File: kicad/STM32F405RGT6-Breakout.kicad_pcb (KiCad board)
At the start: 4 copper layers, 58 parts, among them J1 USB_C_Receptacle_USB2.0, J2 PWR OUT, J3 SWD/JTAG, J4 USART6, J5 SPI1, J6 I2C1, J7 I2C2, Q1 Si2301CDS, SW1 TS-1187A-B-A-B, SW2 TS-1187A-B-A-B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

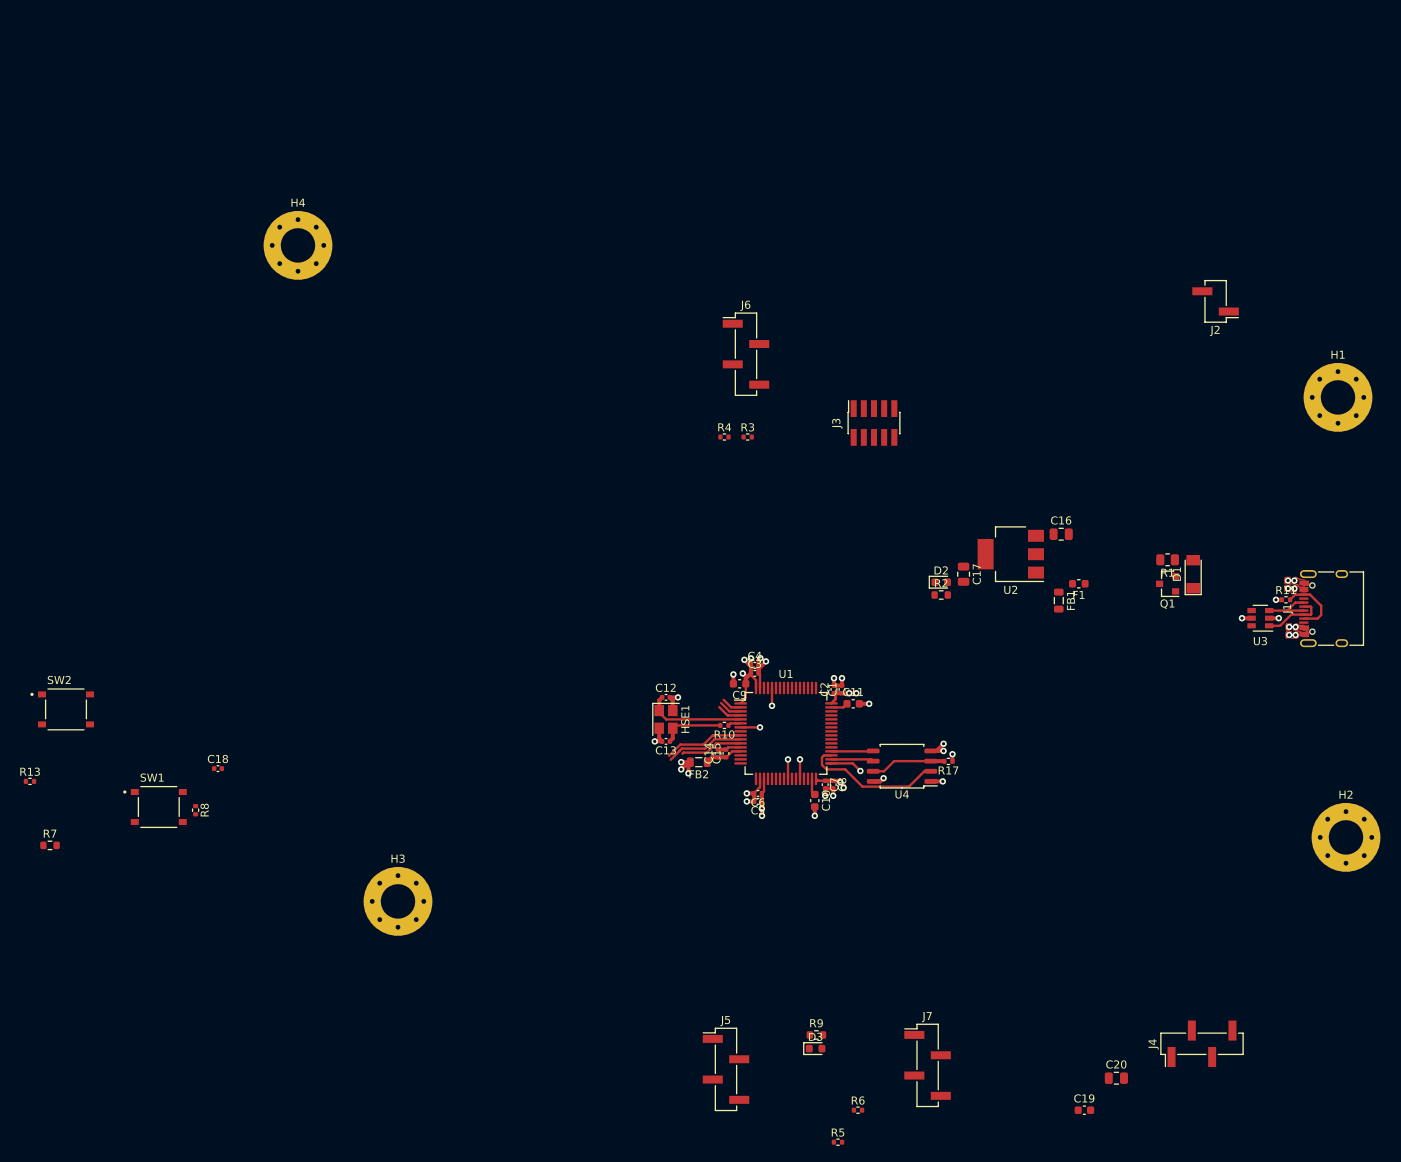
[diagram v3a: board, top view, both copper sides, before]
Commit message: - Lots of GPIO breakouts wired up - Lots of signal isolation vias that I'm completely guessing about
Still to lay out and route: power, USB, UART, SWD
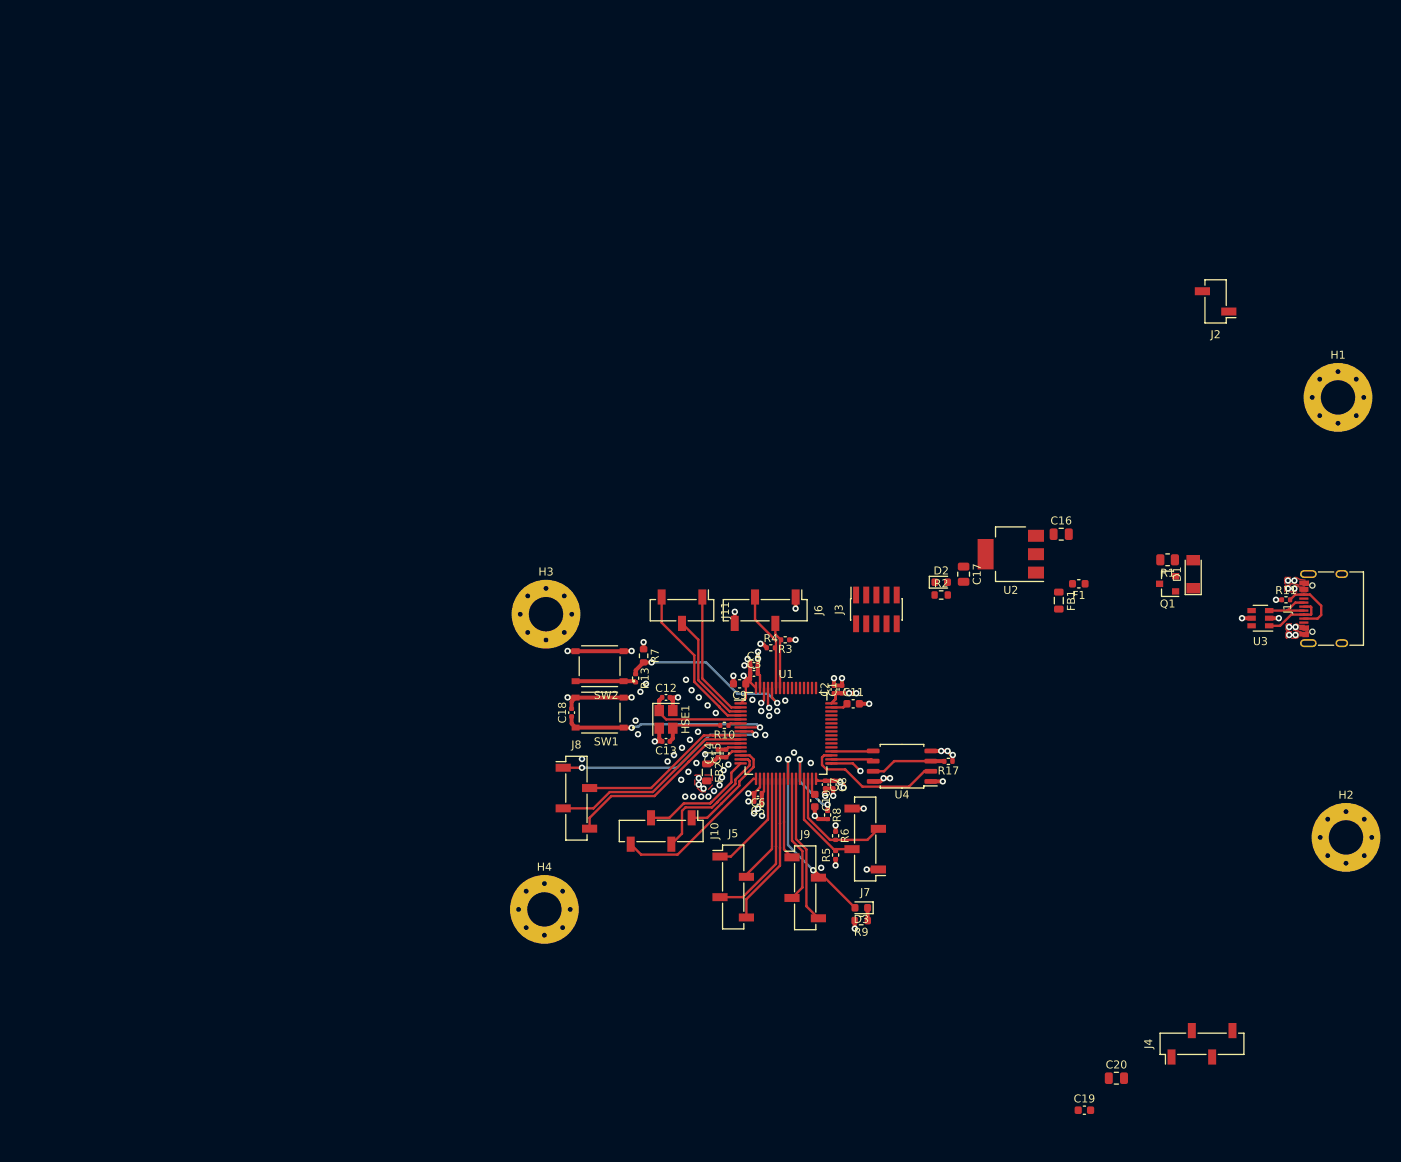
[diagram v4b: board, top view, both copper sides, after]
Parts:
- added J10: Conn_01x04, Connector_PinSocket_2.54mm:PinSocket_1x04_P2.54mm_Vertical_SMD_Pin1Left, F.Cu at (106.4, 97.2)
- added J11: Conn_01x03, Connector_PinSocket_2.54mm:PinSocket_1x03_P2.54mm_Vertical_SMD_Pin1Left, F.Cu at (109.0, 69.6)
- added J8: Conn_01x04, Connector_PinSocket_2.54mm:PinSocket_1x04_P2.54mm_Vertical_SMD_Pin1Left, F.Cu at (95.8, 93.1)
- added J9: Conn_01x04, Connector_PinSocket_2.54mm:PinSocket_1x04_P2.54mm_Vertical_SMD_Pin1Left, F.Cu at (124.4, 104.3)
- J2: footprint Connector_PinHeader_2.54mm:PinHeader_1x02_P2.54mm_Vertical_SMD_Pin1Left -> Connector_PinSocket_2.54mm:PinSocket_1x02_P2.54mm_Vertical_SMD_Pin1Left
- J4, J5, J6, J7: footprint Connector_PinHeader_2.54mm:PinHeader_1x04_P2.54mm_Vertical_SMD_Pin1Left -> Connector_PinSocket_2.54mm:PinSocket_1x04_P2.54mm_Vertical_SMD_Pin1Left
- moved H4 88.5 mm to (91.8, 107.0)
- moved R8 79.0 mm to (127.2, 95.2)
- moved R7 77.9 mm to (104.2, 75.3), turned to 270 degrees
- moved R13 76.8 mm to (103.2, 78.1), turned to 270 degrees
- moved SW2 66.9 mm to (98.7, 76.6), turned to 180 degrees
- moved SW1 56.3 mm to (98.7, 82.4), turned to 180 degrees
- moved C18 44.8 mm to (95.2, 82.4), turned to 90 degrees
- moved H3 40.4 mm to (92.0, 70.1)
- moved R5 35.9 mm to (128.2, 100.2), turned to 90 degrees
- moved R6 34.4 mm to (128.2, 97.8), turned to 270 degrees
- moved J6 32.1 mm to (119.4, 69.6), turned to 270 degrees
- moved J7 29.4 mm to (131.9, 98.2), turned to 180 degrees
- moved R4 27.0 mm to (120.1, 74.3)
- moved R3 25.8 mm to (121.9, 73.3), turned to 180 degrees
- moved J3 23.3 mm to (133.3, 69.5)
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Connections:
- net Net-(D3-Pad2) renamed GPIO_PC5
- U1 pad 10: Net-(U1-Pad10) -> GPIO_PC2
- U1 pad 11: Net-(U1-Pad11) -> GPIO_PC3
- U1 pad 14: Net-(U1-Pad14) -> GPIO_PA0
- U1 pad 15: Net-(U1-Pad15) -> GPIO_PA1
- U1 pad 16: Net-(U1-Pad16) -> GPIO_PA2
- U1 pad 17: Net-(U1-Pad17) -> GPIO_PA3
- U1 pad 2: Net-(U1-Pad2) -> GPIO_PC13
- U1 pad 24: Net-(U1-Pad24) -> GPIO_PC4
- U1 pad 26: Net-(U1-Pad26) -> GPIO_PB0
- U1 pad 27: Net-(U1-Pad27) -> GPIO_PB1
- U1 pad 3: Net-(U1-Pad3) -> GPIO_PC14
- U1 pad 4: Net-(U1-Pad4) -> GPIO_PC15
- U1 pad 8: Net-(U1-Pad8) -> GPIO_PC0
- U1 pad 9: Net-(U1-Pad9) -> GPIO_PC1
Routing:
- net GPIO_PC0: track 0.00 -> 27.8 mm, vias 0 -> 2
- net GPIO_PC2: track 0.00 -> 25.7 mm
- net NRST: track 2.42 -> 27.4 mm, vias 1 -> 2
- net GPIO_PC3: track 0.00 -> 24.1 mm
- net GPIO_PC5: track 2.42 -> 25.3 mm, vias 1 -> 2
- net GPIO_PC1: track 0.00 -> 21.6 mm
- net BOOT0: track 2.22 -> 22.8 mm, vias 1 -> 2
- net GPIO_PA3: track 0.00 -> 20.1 mm
- net GPIO_PC15: track 0.00 -> 19.8 mm
- net SPI1_MISO: track 0.00 -> 19.4 mm
- net SPI1_MOSI: track 0.00 -> 19.1 mm
- net GPIO_PB1: track 0.00 -> 18.6 mm
- net GPIO_PA1: track 0.00 -> 17.6 mm
- net GPIO_PC13: track 0.00 -> 16.5 mm
- net GPIO_PB0: track 0.00 -> 16.0 mm
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- added copper zone on F.Cu, net +3V3
